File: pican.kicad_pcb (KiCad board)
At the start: 4 copper layers, 30 x 65 mm, 37 parts, among them J1 Uart, J2 Conn_01x04_MountingPin, J3 Raspberry_Pi_2_3, J4 Uart, Q1 FDD4243, U1 MCP2558FD-xSN, U2 MCP2515-xSO, U3 R-78B5.0-2.0, U4 LTC280X, Y1 16MHz

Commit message: board nearly finished
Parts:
- added TP2: GND, TestPoint:TestPoint_Keystone_5015_Micro-Minature, B.Cu at (16.5, 32.0)
- TP1: moved to B.Cu
- moved U3 82.6 mm to (24.6, 22.7)
- moved J1 81.8 mm to (12.5, 58.0)
- moved U2 80.8 mm to (13.8, 36.7), turned to 180 degrees
- moved Y1 79.0 mm to (22.1, 35.3), turned to 90 degrees
- moved C6 65.1 mm to (15.6, 19.4), turned to 90 degrees
- moved TP1 62.0 mm to (8.40, 28.7), turned to 90 degrees
- moved C10 61.7 mm to (12.1, 27.2)
- moved FL1 61.2 mm to (26.7, 29.0), turned to 180 degrees
- moved C13 59.3 mm to (20.6, 24.9)
- moved J4 59.0 mm to (25.9, 47.8)
- moved C5 58.7 mm to (27.4, 27.0), turned to 180 degrees
- moved C19 58.6 mm to (20.4, 51.3), turned to -90 degrees
- moved C7 58.3 mm to (23.6, 26.7)
- moved C17 57.9 mm to (17.3, 49.5)
- moved L1 57.1 mm to (22.5, 51.2), turned to -90 degrees
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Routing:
- net +5V: track 0.00 -> 100.5 mm, vias 0 -> 1
- net +3V3: track 0.00 -> 68.7 mm, vias 0 -> 1
- net /RX: track 0.00 -> 56.4 mm
- net /TX: track 0.00 -> 56.2 mm
- net /+12_F: track 0.00 -> 31.4 mm
- net /CAN_TX: track 0.00 -> 21.6 mm
- net /CAN_RX: track 0.00 -> 18.0 mm
- net /RSRX: track 0.00 -> 12.8 mm
- net /OSC_OUT: track 0.00 -> 12.7 mm
- net /RSTX: track 0.00 -> 12.5 mm
- net /CAN_H: track 0.00 -> 10.1 mm
- net /CAN_L: track 0.00 -> 10.1 mm
- net /SPI_MOSI: track 0.00 -> 8.76 mm
- net /SPI_CE0: track 0.00 -> 8.14 mm
- net Net-(C17-Pad2): track 0.00 -> 7.79 mm
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- added copper zone on B.Cu, net GND
- added copper zone on F.Cu, net GND
- added copper zone on In1.Cu, net GND
- added copper zone on In2.Cu, net GND

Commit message: generated bom
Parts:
- added G***: LOGO, ownLib:ownLogoNew, F.Cu at (23.2, 41.6)
- added REF**: OSHW-Logo2_7.3x6mm_SilkScreen, Symbol:OSHW-Logo2_7.3x6mm_SilkScreen, B.Cu at (24.3, 33.4)
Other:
- board text added: "CAN"
- board text added: "CAN Pin: 1 - GND 2 - CAN Low 3 - CAN High 4 - Vcc"
- board text added: "JLCJLCJLCJLC"
- board text added: "RS232"
- board text added: "UART"
- board text added: "github.com/useless-branch - 2021"
- board text added: "piCAN"

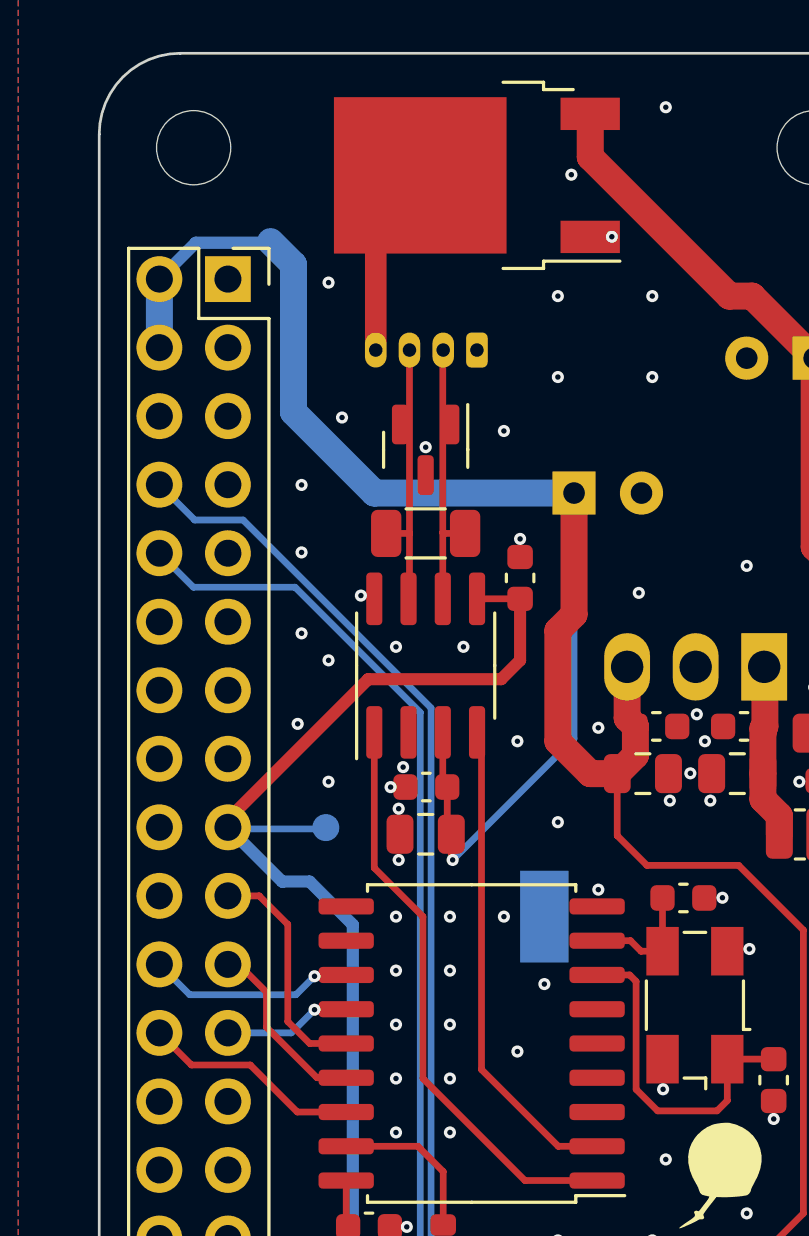
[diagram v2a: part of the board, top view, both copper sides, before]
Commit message: updated board with new connector
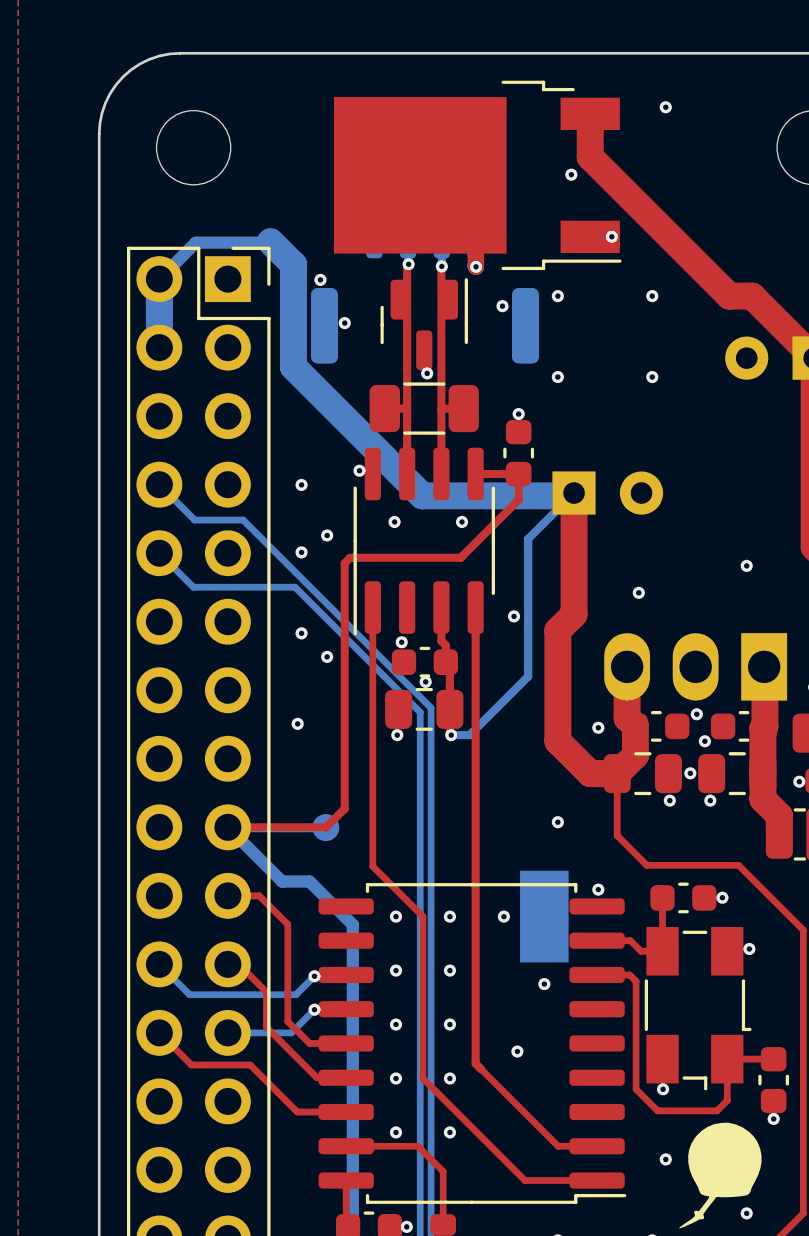
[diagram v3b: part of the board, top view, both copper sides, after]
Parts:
- J2: footprint Connector_Molex:Molex_PicoBlade_53047-0410_1x04_P1.25mm_Vertical -> Connector_Molex:Molex_CLIK-Mate_502382-0470_1x04-1MP_P1.25mm_Vertical
- moved R1 4.63 mm to (12.0, 13.2)
- moved C10 4.63 mm to (12.1, 22.6)
- moved C6 4.63 mm to (15.5, 14.8)
- moved C9 4.63 mm to (12.0, 24.3)
- moved D1 4.63 mm to (12.0, 10.1)
- moved U1 4.63 mm to (12.0, 18.1)
- moved J2 3.00 mm to (12.1, 8.70), turned to 0 degrees
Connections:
- J2 pad 2: /CAN_L -> /CAN_H
- J2 pad 3: /CAN_H -> /CAN_L
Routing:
- net +3V3: track 68.7 -> 74.9 mm
- net +5V: track 100.5 -> 95.4 mm
- net /CAN_TX: track 21.6 -> 26.2 mm
- net /CAN_RX: track 18.0 -> 22.7 mm
- net /12V_IN: track 7.16 -> 5.42 mm, vias 0 -> 1
- net /CAN_L: track 10.1 -> 9.66 mm, vias 0 -> 1
- net /CAN_H: track 10.1 -> 9.73 mm, vias 0 -> 1
- net GND: vias 100 -> 99

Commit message: some stuff!
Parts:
- removed R2: 10k, Resistor_SMD:R_0603_1608Metric
- removed the U1 at (12.0, 18.1)
- added U3: MCP2518FD-xSL, Package_SO:SOIC-14_3.9x8.7mm_P1.27mm, F.Cu at (11.5, 35.2)
- U2: value MCP2515-xSO -> MCP2562FD-E-SN; footprint Package_SO:SOIC-18W_7.5x11.6mm_P1.27mm -> Package_SO:SOIC-8_3.9x4.9mm_P1.27mm
- moved U2 18.7 mm to (12.1, 18.1), turned to 90 degrees
- moved C12 2.84 mm to (9.90, 42.5)
- moved C13 2.82 mm to (9.70, 40.7)
- moved TP2 1.96 mm to (18.4, 32.5)
- moved C2 1.64 mm to (20.1, 31.9)
- moved Y1 1.64 mm to (20.5, 35.8)
- moved C3 1.64 mm to (23.4, 38.6)
- moved G*** 1.57 mm to (22.2, 42.8)
- renumbered C13 to C11, C11 to C12, C12 to C13, C3 to C2, C4 to C3, C2 to C4, U3 to U1
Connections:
- U2 pad 2: /CAN_RX -> GND
- U2 pad 3: unconnected-(U2-Pad3) -> +5V
- U2 pad 4: unconnected-(U2-Pad4) -> /CAN_RX
- U2 pad 5: unconnected-(U2-Pad5) -> +3V3
- U2 pad 6: unconnected-(U2-Pad6) -> /CAN_L
- U2 pad 7: /OSC_OUT -> /CAN_H
- U2 pad 8: /OSC_IN -> GND
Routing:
- net /~{RESET}: track 5.96 -> 0.00 mm
- net /INT: track 7.69 -> 13.2 mm
- net /CAN_TX: track 26.2 -> 21.0 mm
- net /TX: track 56.2 -> 58.8 mm
- net /RX: track 56.4 -> 59.0 mm
- net +3V3: track 74.9 -> 72.4 mm
- net /CAN_RX: track 22.7 -> 20.9 mm
- net /SPI_MISO: track 6.89 -> 5.37 mm
- net /SPI_MOSI: track 8.76 -> 7.48 mm
- net /SPI_CE0: track 8.14 -> 7.39 mm
- net /SPI_SCLK: track 4.75 -> 5.27 mm
- net GND: vias 99 -> 101

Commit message: changed crystal to osc
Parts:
- removed the C2 at (20.1, 31.9)
- removed Y1: 16MHz, ownLib:Crystal_SMD_Abracon_ABM3B-4Pin_5.0x3.2mm
- added R1: 33R, Resistor_SMD:R_0402_1005Metric, F.Cu at (16.2, 32.6)
- added X1: SG-5032CCN, Oscillator:Oscillator_SMD_SeikoEpson_SG8002LB-4Pin_5.0x3.2mm, F.Cu at (19.4, 34.0)
- C3: value 22pF / 10V -> 100nF / 10V
- G***: footprint ownLib:ownLogoNew -> ownLib:LogoMate7x7; moved to B.Cu
- moved C3 4.57 mm to (19.0, 37.5), turned to 0 degrees
- moved G*** 3.68 mm to (23.8, 39.5), turned to -90 degrees
- renumbered C11 to C10, C12 to C11, C13 to C12, C14 to C13, C15 to C14, C16 to C15, C17 to C16, C18 to C17, C19 to C18, C20 to C19, C4 to C2, C5 to C4, C6 to C5, C7 to C6, C8 to C7, C9 to C8, C10 to C9, R1 to R2
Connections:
- C3 pad 1: /OSC_OUT -> +3V3
- U3 pad 6: unconnected-(U3-Pad6) -> Net-(R1-Pad1)
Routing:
- net +3V3: track 72.4 -> 88.9 mm
- net /OSC_OUT: track 12.7 -> 0.00 mm
- net /OSC_IN: track 4.56 -> 0.00 mm
- net Net-(R1-Pad1): track 0.00 -> 1.72 mm
- net Net-(R1-Pad2): track 0.00 -> 1.55 mm
- net GND: vias 101 -> 105
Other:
- outline, holes or cut-outs redrawn
- board text added: "RS232 1 - GND 2 - RSRX 3 - RSTX"
- board text added: "UART 1 - GND 2 - RX 3 - TX"
- board text removed: "JLCJLCJLCJLC"
